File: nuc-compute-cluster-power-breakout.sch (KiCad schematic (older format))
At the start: 4 parts

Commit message: loclib
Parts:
- J? (x2): footprint antmicro-footprints:BM04B-SRSS-TB-LF-SN -> nuc-compute-cluster-power-breakout-footprints:BM04B-SRSS-TB-LF-SN; symbol antmicroRectangularConnectorsHeadersMalePins:BM04B-SRSS-TB-LF-SN -> nuc-compute-cluster-power-breakout:BM04B-SRSS-TB-LF-SN
- R? (x2): footprint antmicro-footprints:0402-res -> nuc-compute-cluster-power-breakout-footprints:0402-res; symbol antmicroResistors0402:R_0R_0402 -> nuc-compute-cluster-power-breakout:R_0R_0402
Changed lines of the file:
@@
 $EndSheet
 $Comp
-L antmicroRectangularConnectorsHeadersMalePins:BM04B-SRSS-TB-LF-SN J?
+L nuc-compute-cluster-power-breakout:BM04B-SRSS-TB-LF-SN J?
 U 1 1 6231F410
 P 2150 2150
 F 0 "J?" H 2100 2500 50  0000 L CNN
 F 1 "BM04B-SRSS-TB-LF-SN" H 2000 2000 50  0000 L CNN
-F 2 "antmicro-footprints:BM04B-SRSS-TB-LF-SN" H 2150 1900 50  0001 C CNN
+F 2 "nuc-compute-cluster-power-breakout-footprints:BM04B-SRSS-TB-LF-SN" H 2150 1900 50  0001 C CNN
 F 3 "https://www.jst-mfg.com/product/pdf/eng/eSH.pdf" H 1700 1850 50  0001 C CNN
 F 4 "BM04B-SRSS-TB(LF)(SN) " H 2050 1800 50  0001 L CNN "MPN"
@@
 $EndComp
 $Comp
-L antmicroRectangularConnectorsHeadersMalePins:BM04B-SRSS-TB-LF-SN J?
+L nuc-compute-cluster-power-breakout:BM04B-SRSS-TB-LF-SN J?
 U 1 1 6231FA57
 P 3900 2150
 F 0 "J?" H 3850 2500 50  0000 L CNN
 F 1 "BM04B-SRSS-TB-LF-SN" H 3750 2000 50  0000 L CNN
-F 2 "antmicro-footprints:BM04B-SRSS-TB-LF-SN" H 3900 1900 50  0001 C CNN
+F 2 "nuc-compute-cluster-power-breakout-footprints:BM04B-SRSS-TB-LF-SN" H 3900 1900 50  0001 C CNN
 F 3 "https://www.jst-mfg.com/product/pdf/eng/eSH.pdf" H 3450 1850 50  0001 C CNN
 F 4 "BM04B-SRSS-TB(LF)(SN) " H 3800 1800 50  0001 L CNN "MPN"
@@
 $EndComp
 $Comp
-L power:GND #PWR?
+L nuc-compute-cluster-power-breakout:GND #PWR?
 U 1 1 6232221D
 P 1800 2300
@@
 	1800 2200 1950 2200
 $Comp
-L power:GND #PWR?
+L nuc-compute-cluster-power-breakout:GND #PWR?
 U 1 1 62322D69
 P 3550 2300
@@
 VCC3V3
 $Comp
-L antmicroResistors0402:R_0R_0402 R?
+L nuc-compute-cluster-power-breakout:R_0R_0402 R?
 U 1 1 62328EB6
 P 1800 1600
 F 0 "R?" V 1755 1670 60  0000 L CNN
 F 1 "R_0R_0402" H 1800 1450 60  0001 C CNN
-F 2 "antmicro-footprints:0402-res" H 2000 1800 60  0001 L CNN
+F 2 "nuc-compute-cluster-power-breakout-footprints:0402-res" H 2000 1800 60  0001 L CNN
 F 3 "" H 1800 1600 50  0001 C CNN
 F 4 "PANASONIC" H 2000 2000 60  0001 L CNN "Manufacturer"
@@
 $EndComp
 $Comp
-L antmicroResistors0402:R_0R_0402 R?
+L nuc-compute-cluster-power-breakout:R_0R_0402 R?
 U 1 1 62329827
 P 3550 1600
 F 0 "R?" V 3505 1670 60  0000 L CNN
 F 1 "R_0R_0402" H 3550 1450 60  0001 C CNN
-F 2 "antmicro-footprints:0402-res" H 3750 1800 60  0001 L CNN
+F 2 "nuc-compute-cluster-power-breakout-footprints:0402-res" H 3750 1800 60  0001 L CNN
 F 3 "" H 3550 1600 50  0001 C CNN
 F 4 "PANASONIC" H 3750 2000 60  0001 L CNN "Manufacturer"

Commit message: Added power connectors
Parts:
- added U? (x4), U??: 430450812, symbol antmicroRectangularConnectorsHeadersFemalePins:430450812
- J? (x2): footprint nuc-compute-cluster-power-breakout-footprints:BM04B-SRSS-TB-LF-SN -> antmicro-footprints:BM04B-SRSS-TB-LF-SN; symbol nuc-compute-cluster-power-breakout:BM04B-SRSS-TB-LF-SN -> antmicroRectangularConnectorsHeadersMalePins:BM04B-SRSS-TB-LF-SN
- R? (x2): footprint nuc-compute-cluster-power-breakout-footprints:0402-res -> antmicro-footprints:0402-res; symbol nuc-compute-cluster-power-breakout:R_0R_0402 -> antmicroResistors0402:R_0R_0402
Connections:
- net GND: now also U?.5, U?.5, U?.5, U?.5, U?.6, U?.6, U?.6, U?.6, U?.7, U?.7, U?.7, U?.7, U?.8, U?.8, U?.8, U?.8, U??.5, U??.6, U??.7, U??.8
- new net LOAD_1: U??.1, U??.2, U??.3, U??.4
- new net LOAD_2: U?.1, U?.2, U?.3, U?.4
- new net LOAD_3: U?.1, U?.2, U?.3, U?.4
- new net LOAD_4: U?.1, U?.2, U?.3, U?.4
- new net LOAD_5: U?.1, U?.2, U?.3, U?.4

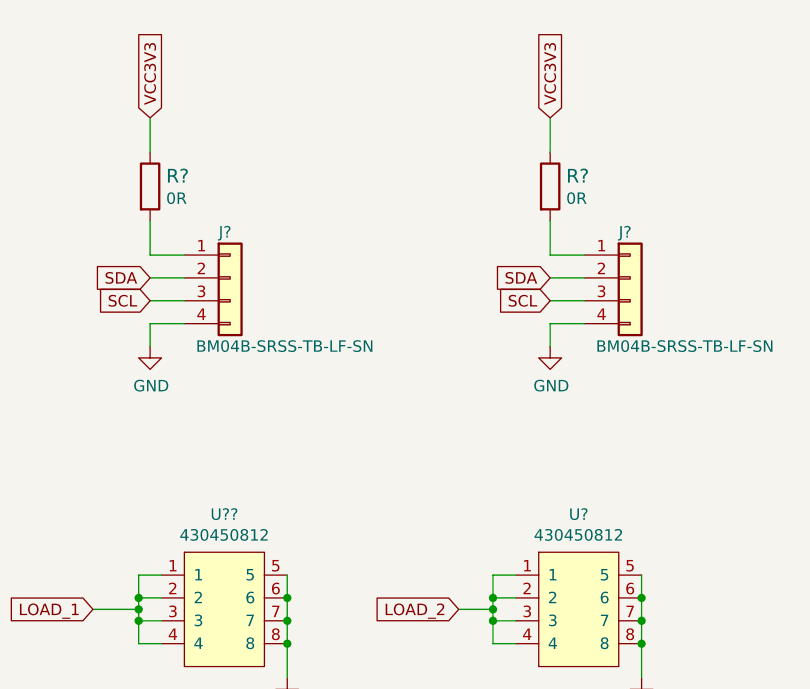
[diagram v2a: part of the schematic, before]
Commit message: Added power distribution connectors
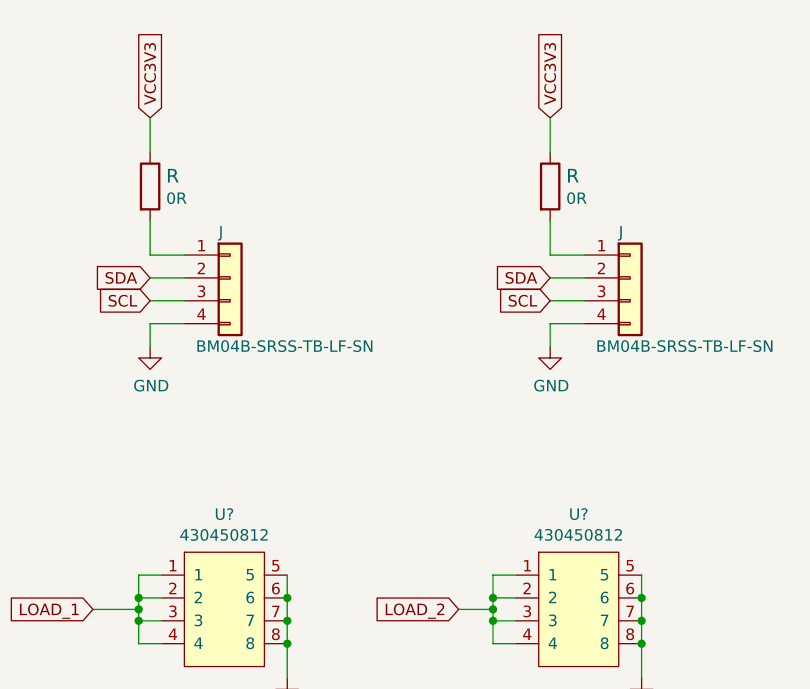
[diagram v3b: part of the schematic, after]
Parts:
- U?: renamed from U??; footprint (none) -> antmicro-footprints:Molex-43045-0812
- U? (x4): footprint (none) -> antmicro-footprints:Molex-43045-0812
- gave numbers to parts that had none: 2
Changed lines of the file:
@@
 $EndSheet
 $Comp
-L antmicroRectangularConnectorsHeadersMalePins:BM04B-SRSS-TB-LF-SN J?
+L antmicroRectangularConnectorsHeadersMalePins:BM04B-SRSS-TB-LF-SN J
 U 1 1 6231F410
 P 2150 2150
-F 0 "J?" H 2100 2500 50  0000 L CNN
+F 0 "J" H 2100 2500 50  0000 L CNN
 F 1 "BM04B-SRSS-TB-LF-SN" H 2000 2000 50  0000 L CNN
 F 2 "antmicro-footprints:BM04B-SRSS-TB-LF-SN" H 2150 1900 50  0001 C CNN
@@
 $EndComp
 $Comp
-L antmicroRectangularConnectorsHeadersMalePins:BM04B-SRSS-TB-LF-SN J?
+L antmicroRectangularConnectorsHeadersMalePins:BM04B-SRSS-TB-LF-SN J
 U 1 1 6231FA57
 P 3900 2150
-F 0 "J?" H 3850 2500 50  0000 L CNN
+F 0 "J" H 3850 2500 50  0000 L CNN
 F 1 "BM04B-SRSS-TB-LF-SN" H 3750 2000 50  0000 L CNN
 F 2 "antmicro-footprints:BM04B-SRSS-TB-LF-SN" H 3900 1900 50  0001 C CNN
@@
 $EndComp
 $Comp
-L power:GND #PWR?
+L power:GND #PWR
 U 1 1 6232221D
 P 1800 2300
-F 0 "#PWR?" H 1800 2050 50  0001 C CNN
+F 0 "#PWR" H 1800 2050 50  0001 C CNN
 F 1 "GND" H 1805 2127 50  0000 C CNN
 F 2 "" H 1800 2300 50  0001 C CNN
@@
 	1800 2200 1950 2200
 $Comp
-L power:GND #PWR?
+L power:GND #PWR
 U 1 1 62322D69
 P 3550 2300
-F 0 "#PWR?" H 3550 2050 50  0001 C CNN
+F 0 "#PWR" H 3550 2050 50  0001 C CNN
 F 1 "GND" H 3555 2127 50  0000 C CNN
 F 2 "" H 3550 2300 50  0001 C CNN
@@
 VCC3V3
 $Comp
-L antmicroResistors0402:R_0R_0402 R?
+L antmicroResistors0402:R_0R_0402 R
 U 1 1 62328EB6
 P 1800 1600
-F 0 "R?" V 1755 1670 60  0000 L CNN
+F 0 "R" V 1755 1670 60  0000 L CNN
 F 1 "R_0R_0402" H 1800 1450 60  0001 C CNN
 F 2 "antmicro-footprints:0402-res" H 2000 1800 60  0001 L CNN
@@
 $EndComp
 $Comp
-L antmicroResistors0402:R_0R_0402 R?
+L antmicroResistors0402:R_0R_0402 R
 U 1 1 62329827
 P 3550 1600
-F 0 "R?" V 3505 1670 60  0000 L CNN
+F 0 "R" V 3505 1670 60  0000 L CNN
 F 1 "R_0R_0402" H 3550 1450 60  0001 C CNN
 F 2 "antmicro-footprints:0402-res" H 3750 1800 60  0001 L CNN
@@
 $EndBitmap
 $Comp
-L antmicroRectangularConnectorsHeadersFemalePins:430450812 U??
+L antmicroRectangularConnectorsHeadersFemalePins:430450812 U?
 U 1 1 62389198
 P 2100 3300
-F 0 "U??" H 2125 3565 50  0000 C CNN
+F 0 "U?" H 2125 3565 50  0000 C CNN
 F 1 "430450812" H 2125 3474 50  0000 C CNN
-F 2 "" H 1950 3300 50  0001 C CNN
+F 2 "antmicro-footprints:Molex-43045-0812" H 1950 3300 50  0001 C CNN
 F 3 "https://www.molex.com/pdm_docs/sd/430450812_sd.pdf" H 1950 3300 50  0001 C CNN
 F 4 "430450812" H 2100 3300 50  0001 C CNN "MPN"
@@
 F 0 "U?" H 3675 3565 50  0000 C CNN
 F 1 "430450812" H 3675 3474 50  0000 C CNN
-F 2 "" H 3500 3300 50  0001 C CNN
+F 2 "antmicro-footprints:Molex-43045-0812" H 3500 3300 50  0001 C CNN
 F 3 "https://www.molex.com/pdm_docs/sd/430450812_sd.pdf" H 3500 3300 50  0001 C CNN
 F 4 "430450812" H 3650 3300 50  0001 C CNN "MPN"
@@
 F 0 "U?" H 2125 4515 50  0000 C CNN
 F 1 "430450812" H 2125 4424 50  0000 C CNN
-F 2 "" H 1950 4250 50  0001 C CNN
+F 2 "antmicro-footprints:Molex-43045-0812" H 1950 4250 50  0001 C CNN
 F 3 "https://www.molex.com/pdm_docs/sd/430450812_sd.pdf" H 1950 4250 50  0001 C CNN
 F 4 "430450812" H 2100 4250 50  0001 C CNN "MPN"
@@
 F 0 "U?" H 3675 4515 50  0000 C CNN
 F 1 "430450812" H 3675 4424 50  0000 C CNN
-F 2 "" H 3500 4250 50  0001 C CNN
+F 2 "antmicro-footprints:Molex-43045-0812" H 3500 4250 50  0001 C CNN
 F 3 "https://www.molex.com/pdm_docs/sd/430450812_sd.pdf" H 3500 4250 50  0001 C CNN
 F 4 "430450812" H 3650 4250 50  0001 C CNN "MPN"
@@
 F 0 "U?" H 2875 5665 50  0000 C CNN
 F 1 "430450812" H 2875 5574 50  0000 C CNN
-F 2 "" H 2700 5400 50  0001 C CNN
+F 2 "antmicro-footprints:Molex-43045-0812" H 2700 5400 50  0001 C CNN
 F 3 "https://www.molex.com/pdm_docs/sd/430450812_sd.pdf" H 2700 5400 50  0001 C CNN
 F 4 "430450812" H 2850 5400 50  0001 C CNN "MPN"
@@
 	1750 3450 1750 3400
 $Comp
-L power:GND #PWR?
+L power:GND #PWR
 U 1 1 62392E27
 P 2400 3750
-F 0 "#PWR?" H 2400 3500 50  0001 C CNN
+F 0 "#PWR" H 2400 3500 50  0001 C CNN
 F 1 "GND" H 2405 3577 50  0000 C CNN
 F 2 "" H 2400 3750 50  0001 C CNN
@@
 	2400 3600 2400 3500
 $Comp
-L power:GND #PWR?
+L power:GND #PWR
 U 1 1 62394589
 P 2400 4800
-F 0 "#PWR?" H 2400 4550 50  0001 C CNN
+F 0 "#PWR" H 2400 4550 50  0001 C CNN
 F 1 "GND" H 2405 4627 50  0000 C CNN
 F 2 "" H 2400 4800 50  0001 C CNN
@@
 	2400 4550 2400 4450
 $Comp
-L power:GND #PWR?
+L power:GND #PWR
 U 1 1 6239614B
 P 3950 4800
-F 0 "#PWR?" H 3950 4550 50  0001 C CNN
+F 0 "#PWR" H 3950 4550 50  0001 C CNN
 F 1 "GND" H 3955 4627 50  0000 C CNN
 F 2 "" H 3950 4800 50  0001 C CNN
@@
 	3950 4550 3950 4450
 $Comp
-L power:GND #PWR?
+L power:GND #PWR
 U 1 1 62398F4B
 P 3150 6000
-F 0 "#PWR?" H 3150 5750 50  0001 C CNN
+F 0 "#PWR" H 3150 5750 50  0001 C CNN
 F 1 "GND" H 3155 5827 50  0000 C CNN
 F 2 "" H 3150 6000 50  0001 C CNN
@@
 	3150 5700 3150 5600
 $Comp
-L power:GND #PWR?
+L power:GND #PWR
 U 1 1 62399AC9
 P 3950 3750
-F 0 "#PWR?" H 3950 3500 50  0001 C CNN
+F 0 "#PWR" H 3950 3500 50  0001 C CNN
 F 1 "GND" H 3955 3577 50  0000 C CNN
 F 2 "" H 3950 3750 50  0001 C CNN

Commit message: Schematic complete
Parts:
- gave numbers to parts that had none: 5
- renumbered J to J2, J to J3, R to R10, R to R9
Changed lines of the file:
@@
 $EndSheet
 $Comp
-L antmicroRectangularConnectorsHeadersMalePins:BM04B-SRSS-TB-LF-SN J
+L antmicroRectangularConnectorsHeadersMalePins:BM04B-SRSS-TB-LF-SN J2
 U 1 1 6231F410
 P 2150 2150
-F 0 "J" H 2100 2500 50  0000 L CNN
+F 0 "J2" H 2100 2500 50  0000 L CNN
 F 1 "BM04B-SRSS-TB-LF-SN" H 2000 2000 50  0000 L CNN
 F 2 "antmicro-footprints:BM04B-SRSS-TB-LF-SN" H 2150 1900 50  0001 C CNN
@@
 $EndComp
 $Comp
-L antmicroRectangularConnectorsHeadersMalePins:BM04B-SRSS-TB-LF-SN J
+L antmicroRectangularConnectorsHeadersMalePins:BM04B-SRSS-TB-LF-SN J3
 U 1 1 6231FA57
 P 3900 2150
-F 0 "J" H 3850 2500 50  0000 L CNN
+F 0 "J3" H 3850 2500 50  0000 L CNN
 F 1 "BM04B-SRSS-TB-LF-SN" H 3750 2000 50  0000 L CNN
 F 2 "antmicro-footprints:BM04B-SRSS-TB-LF-SN" H 3900 1900 50  0001 C CNN
@@
 $EndComp
 $Comp
-L power:GND #PWR
+L power:GND #PWR023
 U 1 1 6232221D
 P 1800 2300
-F 0 "#PWR" H 1800 2050 50  0001 C CNN
+F 0 "#PWR023" H 1800 2050 50  0001 C CNN
 F 1 "GND" H 1805 2127 50  0000 C CNN
 F 2 "" H 1800 2300 50  0001 C CNN
@@
 	1800 2200 1950 2200
 $Comp
-L power:GND #PWR
+L power:GND #PWR033
 U 1 1 62322D69
 P 3550 2300
-F 0 "#PWR" H 3550 2050 50  0001 C CNN
+F 0 "#PWR033" H 3550 2050 50  0001 C CNN
 F 1 "GND" H 3555 2127 50  0000 C CNN
 F 2 "" H 3550 2300 50  0001 C CNN
@@
 VCC3V3
 $Comp
-L antmicroResistors0402:R_0R_0402 R
+L antmicroResistors0402:R_0R_0402 R9
 U 1 1 62328EB6
 P 1800 1600
-F 0 "R" V 1755 1670 60  0000 L CNN
+F 0 "R9" V 1755 1670 60  0000 L CNN
 F 1 "R_0R_0402" H 1800 1450 60  0001 C CNN
 F 2 "antmicro-footprints:0402-res" H 2000 1800 60  0001 L CNN
@@
 $EndComp
 $Comp
-L antmicroResistors0402:R_0R_0402 R
+L antmicroResistors0402:R_0R_0402 R10
 U 1 1 62329827
 P 3550 1600
-F 0 "R" V 3505 1670 60  0000 L CNN
+F 0 "R10" V 3505 1670 60  0000 L CNN
 F 1 "R_0R_0402" H 3550 1450 60  0001 C CNN
 F 2 "antmicro-footprints:0402-res" H 3750 1800 60  0001 L CNN
@@
 $EndBitmap
 $Comp
-L antmicroRectangularConnectorsHeadersFemalePins:430450812 U?
+L antmicroRectangularConnectorsHeadersFemalePins:430450812 U2
 U 1 1 62389198
 P 2100 3300
-F 0 "U?" H 2125 3565 50  0000 C CNN
+F 0 "U2" H 2125 3565 50  0000 C CNN
 F 1 "430450812" H 2125 3474 50  0000 C CNN
 F 2 "antmicro-footprints:Molex-43045-0812" H 1950 3300 50  0001 C CNN
@@
 $EndComp
 $Comp
-L antmicroRectangularConnectorsHeadersFemalePins:430450812 U?
+L antmicroRectangularConnectorsHeadersFemalePins:430450812 U5
 U 1 1 623895A5
 P 3650 3300
-F 0 "U?" H 3675 3565 50  0000 C CNN
+F 0 "U5" H 3675 3565 50  0000 C CNN
 F 1 "430450812" H 3675 3474 50  0000 C CNN
 F 2 "antmicro-footprints:Molex-43045-0812" H 3500 3300 50  0001 C CNN
@@
 $EndComp
 $Comp
-L antmicroRectangularConnectorsHeadersFemalePins:430450812 U?
+L antmicroRectangularConnectorsHeadersFemalePins:430450812 U3
 U 1 1 6238989A
 P 2100 4250
-F 0 "U?" H 2125 4515 50  0000 C CNN
+F 0 "U3" H 2125 4515 50  0000 C CNN
 F 1 "430450812" H 2125 4424 50  0000 C CNN
 F 2 "antmicro-footprints:Molex-43045-0812" H 1950 4250 50  0001 C CNN
@@
 $EndComp
 $Comp
-L antmicroRectangularConnectorsHeadersFemalePins:430450812 U?
+L antmicroRectangularConnectorsHeadersFemalePins:430450812 U6
 U 1 1 62389AA4
 P 3650 4250
-F 0 "U?" H 3675 4515 50  0000 C CNN
+F 0 "U6" H 3675 4515 50  0000 C CNN
 F 1 "430450812" H 3675 4424 50  0000 C CNN
 F 2 "antmicro-footprints:Molex-43045-0812" H 3500 4250 50  0001 C CNN
@@
 $EndComp
 $Comp
-L antmicroRectangularConnectorsHeadersFemalePins:430450812 U?
+L antmicroRectangularConnectorsHeadersFemalePins:430450812 U4
 U 1 1 62389CDB
 P 2850 5400
-F 0 "U?" H 2875 5665 50  0000 C CNN
+F 0 "U4" H 2875 5665 50  0000 C CNN
 F 1 "430450812" H 2875 5574 50  0000 C CNN
 F 2 "antmicro-footprints:Molex-43045-0812" H 2700 5400 50  0001 C CNN
@@
 	1750 3450 1750 3400
 $Comp
-L power:GND #PWR
+L power:GND #PWR027
 U 1 1 62392E27
 P 2400 3750
-F 0 "#PWR" H 2400 3500 50  0001 C CNN
+F 0 "#PWR027" H 2400 3500 50  0001 C CNN
 F 1 "GND" H 2405 3577 50  0000 C CNN
 F 2 "" H 2400 3750 50  0001 C CNN
@@
 	2400 3600 2400 3500
 $Comp
-L power:GND #PWR
+L power:GND #PWR030
 U 1 1 62394589
 P 2400 4800
-F 0 "#PWR" H 2400 4550 50  0001 C CNN
+F 0 "#PWR030" H 2400 4550 50  0001 C CNN
 F 1 "GND" H 2405 4627 50  0000 C CNN
 F 2 "" H 2400 4800 50  0001 C CNN
@@
 	2400 4550 2400 4450
 $Comp
-L power:GND #PWR
+L power:GND #PWR035
 U 1 1 6239614B
 P 3950 4800
-F 0 "#PWR" H 3950 4550 50  0001 C CNN
+F 0 "#PWR035" H 3950 4550 50  0001 C CNN
 F 1 "GND" H 3955 4627 50  0000 C CNN
 F 2 "" H 3950 4800 50  0001 C CNN
@@
 	3950 4550 3950 4450
 $Comp
-L power:GND #PWR
+L power:GND #PWR031
 U 1 1 62398F4B
 P 3150 6000
-F 0 "#PWR" H 3150 5750 50  0001 C CNN
+F 0 "#PWR031" H 3150 5750 50  0001 C CNN
 F 1 "GND" H 3155 5827 50  0000 C CNN
 F 2 "" H 3150 6000 50  0001 C CNN
@@
 	3150 5700 3150 5600
 $Comp
-L power:GND #PWR
+L power:GND #PWR034
 U 1 1 62399AC9
 P 3950 3750
-F 0 "#PWR" H 3950 3500 50  0001 C CNN
+F 0 "#PWR034" H 3950 3500 50  0001 C CNN
 F 1 "GND" H 3955 3577 50  0000 C CNN
 F 2 "" H 3950 3750 50  0001 C CNN

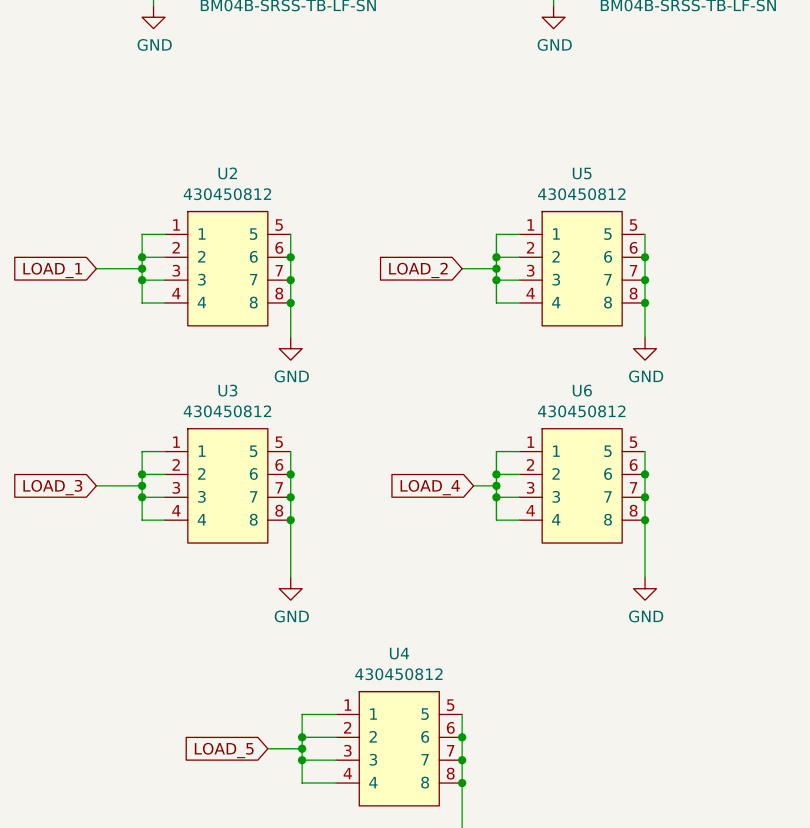
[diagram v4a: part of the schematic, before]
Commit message: PCB creation. Components gathered in functional groups
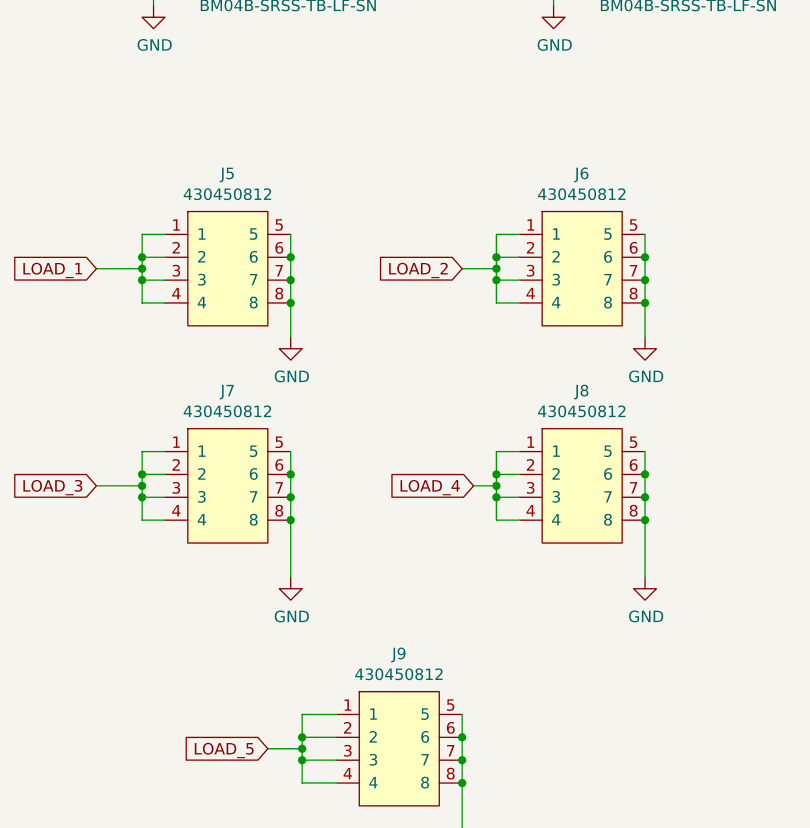
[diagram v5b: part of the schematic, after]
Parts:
- renumbered U2 to J5, U5 to J6, U3 to J7, U6 to J8, U4 to J9
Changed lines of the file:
@@
 $EndBitmap
 $Comp
-L antmicroRectangularConnectorsHeadersFemalePins:430450812 U2
+L antmicroRectangularConnectorsHeadersFemalePins:430450812 J5
 U 1 1 62389198
 P 2100 3300
-F 0 "U2" H 2125 3565 50  0000 C CNN
+F 0 "J5" H 2125 3565 50  0000 C CNN
 F 1 "430450812" H 2125 3474 50  0000 C CNN
 F 2 "antmicro-footprints:Molex-43045-0812" H 1950 3300 50  0001 C CNN
@@
 $EndComp
 $Comp
-L antmicroRectangularConnectorsHeadersFemalePins:430450812 U5
+L antmicroRectangularConnectorsHeadersFemalePins:430450812 J6
 U 1 1 623895A5
 P 3650 3300
-F 0 "U5" H 3675 3565 50  0000 C CNN
+F 0 "J6" H 3675 3565 50  0000 C CNN
 F 1 "430450812" H 3675 3474 50  0000 C CNN
 F 2 "antmicro-footprints:Molex-43045-0812" H 3500 3300 50  0001 C CNN
@@
 $EndComp
 $Comp
-L antmicroRectangularConnectorsHeadersFemalePins:430450812 U3
+L antmicroRectangularConnectorsHeadersFemalePins:430450812 J7
 U 1 1 6238989A
 P 2100 4250
-F 0 "U3" H 2125 4515 50  0000 C CNN
+F 0 "J7" H 2125 4515 50  0000 C CNN
 F 1 "430450812" H 2125 4424 50  0000 C CNN
 F 2 "antmicro-footprints:Molex-43045-0812" H 1950 4250 50  0001 C CNN
@@
 $EndComp
 $Comp
-L antmicroRectangularConnectorsHeadersFemalePins:430450812 U6
+L antmicroRectangularConnectorsHeadersFemalePins:430450812 J8
 U 1 1 62389AA4
 P 3650 4250
-F 0 "U6" H 3675 4515 50  0000 C CNN
+F 0 "J8" H 3675 4515 50  0000 C CNN
 F 1 "430450812" H 3675 4424 50  0000 C CNN
 F 2 "antmicro-footprints:Molex-43045-0812" H 3500 4250 50  0001 C CNN
@@
 $EndComp
 $Comp
-L antmicroRectangularConnectorsHeadersFemalePins:430450812 U4
+L antmicroRectangularConnectorsHeadersFemalePins:430450812 J9
 U 1 1 62389CDB
 P 2850 5400
-F 0 "U4" H 2875 5665 50  0000 C CNN
+F 0 "J9" H 2875 5665 50  0000 C CNN
 F 1 "430450812" H 2875 5574 50  0000 C CNN
 F 2 "antmicro-footprints:Molex-43045-0812" H 2700 5400 50  0001 C CNN
